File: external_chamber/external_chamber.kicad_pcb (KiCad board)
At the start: 2 copper layers, 76.2 x 106.4 mm, 15 parts, among them J1 9, J2 5, J3 4, J4 1, J5 2, J6 8, J7 3, J8 6, J9 Conn_01x02_Socket, U1 CY8CKIT-059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

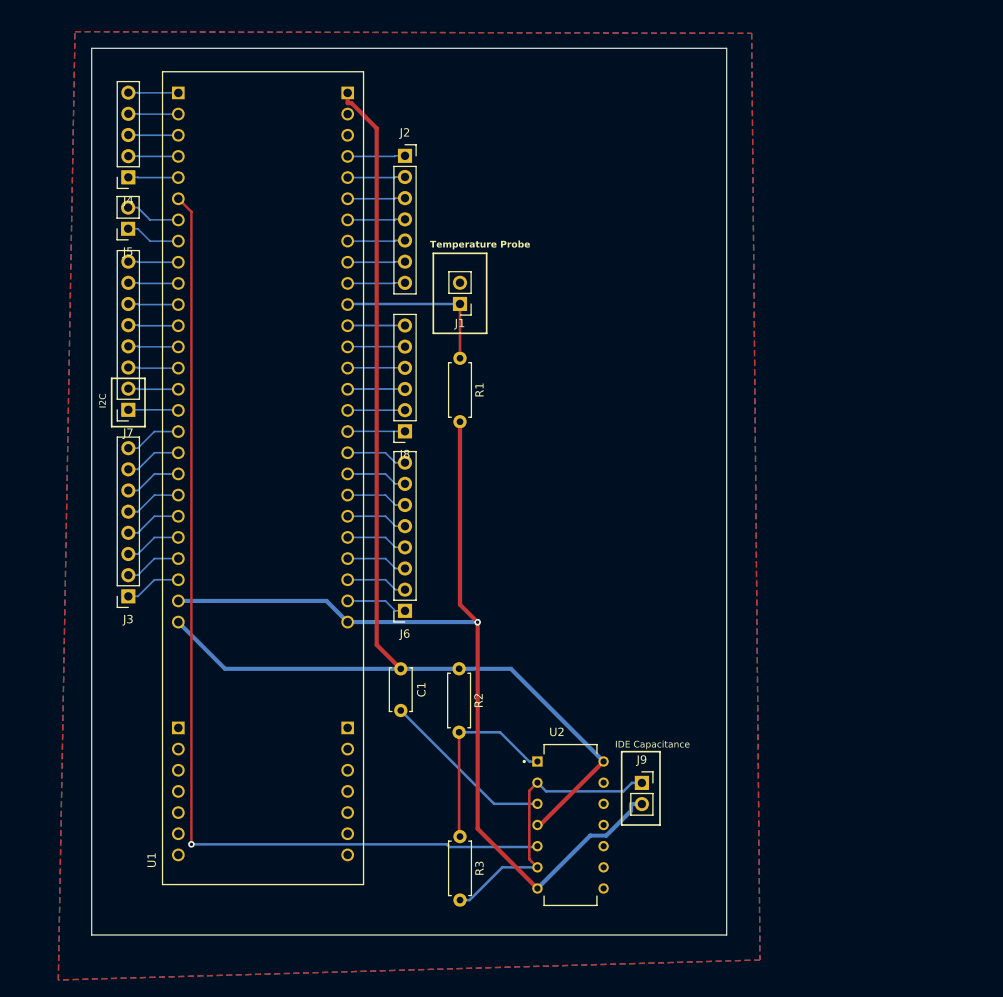
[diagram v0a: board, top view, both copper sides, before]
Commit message: Updated heater controls and uploaded re-design of external chamber PCB
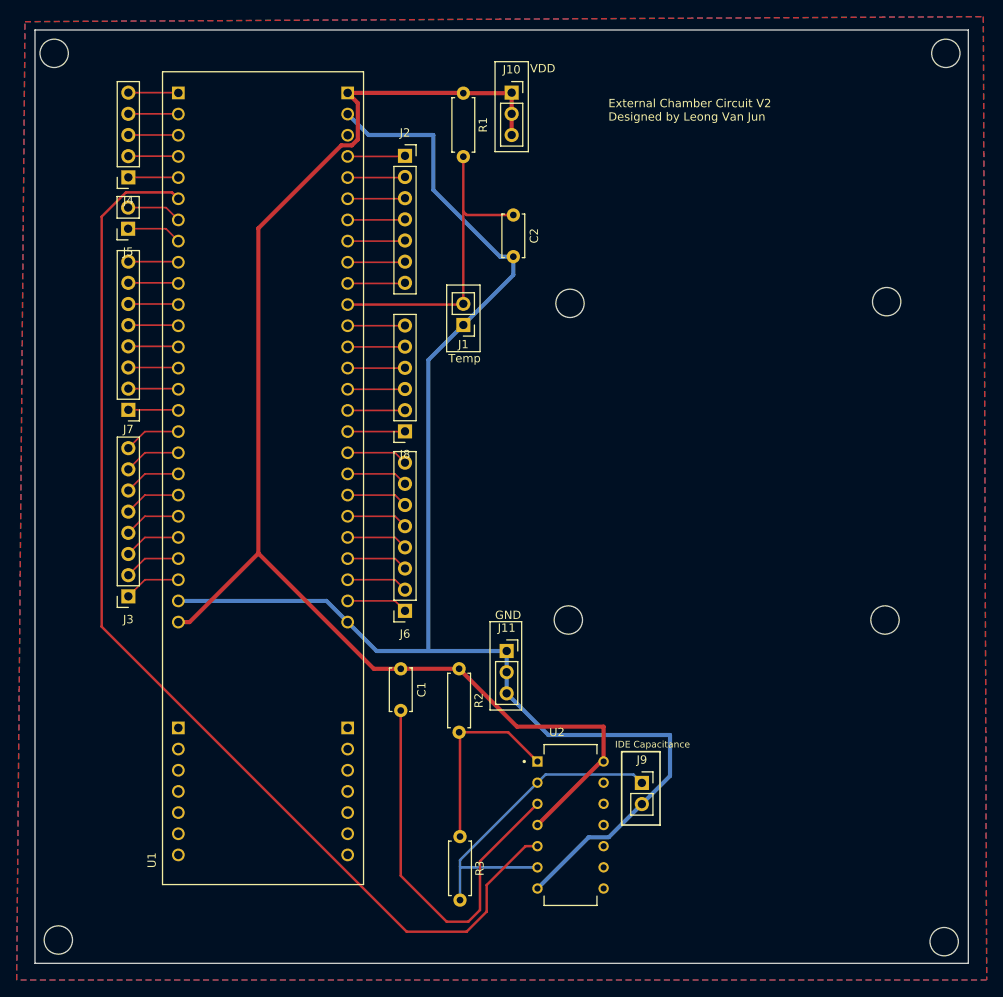
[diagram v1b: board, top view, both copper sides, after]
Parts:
- added C2: 100n, Capacitor_THT:C_Disc_D5.0mm_W2.5mm_P5.00mm, F.Cu at (131.2, 69.4)
- added J10: Conn_01x03_Pin, Connector_PinSocket_2.54mm:PinSocket_1x03_P2.54mm_Vertical, F.Cu at (131.0, 54.7)
- added J11: Conn_01x03_Pin, Connector_PinSocket_2.54mm:PinSocket_1x03_P2.54mm_Vertical, F.Cu at (130.4, 121.7)
- J1: value 9 -> Conn_01x02_Socket
- J2: value 5 -> Conn_01x07_Socket
- J3: value 4 -> Conn_01x08_Socket
- J4: value 1 -> Conn_01x05_Socket
- J5: value 2 -> Conn_01x02_Socket
- J6: value 8 -> Conn_01x08_Socket
- J7: value 3 -> Conn_01x08_Socket; footprint Connector_PinSocket_2.54mm:PinSocket_1x08_P2.54mm_Vertical -> Connector_PinHeader_2.54mm:PinHeader_1x08_P2.54mm_Vertical
- J8: value 6 -> Conn_01x06_Socket
- moved R1 31.8 mm to (125.2, 54.8)
- moved J1 2.56 mm to (125.2, 82.6)
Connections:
- J1 pad 1: /Temp -> GND
- J1 pad 2: unconnected-(J1-Pin_2-Pad2) -> /Temp
- R1 pad 1: /Temp -> +5V
- R1 pad 2: GND -> /Temp
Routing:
- net GND: track 114.0 -> 177.4 mm, vias 1 -> 0
- net /TimerCont: track 21.0 -> 47.8 mm
- net +5V: track 141.1 -> 164.6 mm
- net /Temp: track 20.0 -> 37.7 mm
- net /TimerOut: track 119.8 -> 133.5 mm, vias 1 -> 0
- net /TimerThresh: track 35.3 -> 40.6 mm
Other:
- board size 76.2 x 106.4 mm -> 112 x 112 mm
- board text added: "External Chamber Circuit V2 Designed by Leong Van Jun"
- board text added: "GND"
- board text added: "Temp"
- board text added: "VDD"
- board text removed: "I2C"
- board text removed: "Temperature Probe"
